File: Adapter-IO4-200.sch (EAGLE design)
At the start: 3 parts, among them X1 MSTBA6

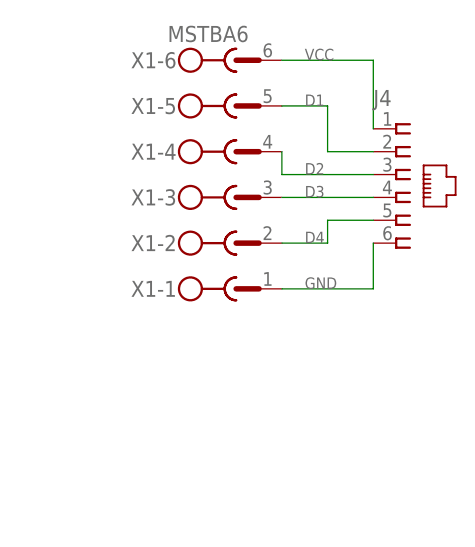
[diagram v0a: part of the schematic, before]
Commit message: added values for connectors
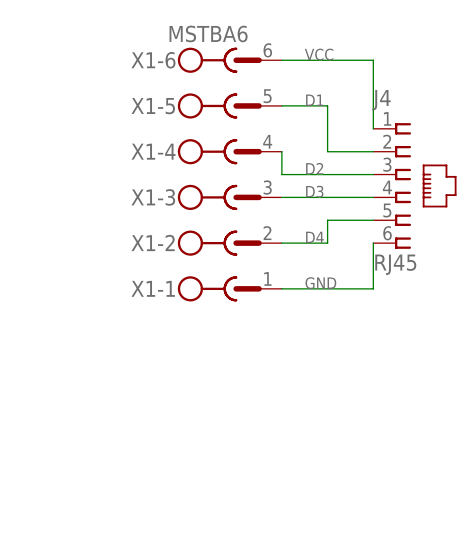
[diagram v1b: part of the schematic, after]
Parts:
- J4: value (none) -> RJ45
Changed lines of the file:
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@@
 <part name="FRAME1" library="SparkFun" deviceset="FRAME-LETTER" device=""/>
 <part name="U$1" library="SparkFun" deviceset="OSHW-LOGO" device="M"/>
-<part name="J4" library="SPCoast" deviceset="CONNECTOR-RJ25" device="-6P6C"/>
+<part name="J4" library="SPCoast" deviceset="CONNECTOR-RJ25" device="-6P6C" value="RJ45"/>
 <part name="X1" library="con-phoenix-508" deviceset="MSTBA6" device=""/>
 </parts>

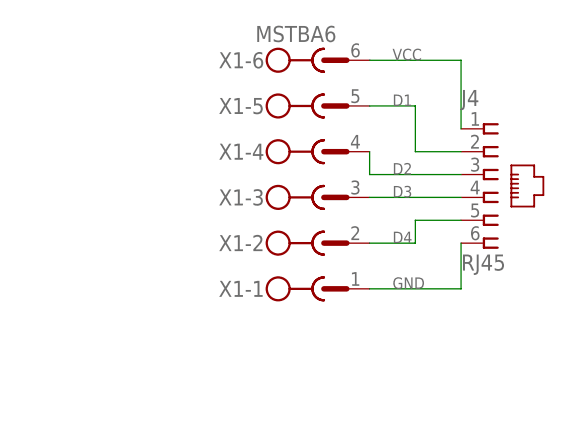
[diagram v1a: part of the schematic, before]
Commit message: normalized values
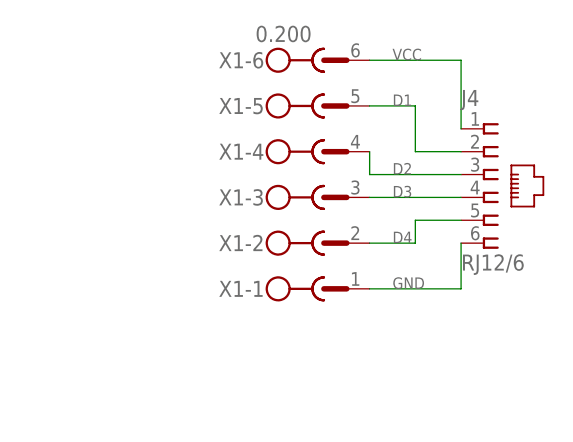
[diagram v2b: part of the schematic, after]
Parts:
- J4: value RJ45 -> RJ12/6
- U$1: value OSHW-LOGOM -> OSHW
- X1: value MSTBA6 -> 0.200
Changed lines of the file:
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@@
 <parts>
 <part name="FRAME1" library="SparkFun" deviceset="FRAME-LETTER" device=""/>
-<part name="U$1" library="SparkFun" deviceset="OSHW-LOGO" device="M"/>
-<part name="J4" library="SPCoast" deviceset="CONNECTOR-RJ25" device="-6P6C" value="RJ45"/>
-<part name="X1" library="con-phoenix-508" deviceset="MSTBA6" device=""/>
+<part name="U$1" library="SparkFun" deviceset="OSHW-LOGO" device="M" value="OSHW"/>
+<part name="J4" library="SPCoast" deviceset="CONNECTOR-RJ25" device="-6P6C" value="RJ12/6"/>
+<part name="X1" library="con-phoenix-508" deviceset="MSTBA6" device="" value="0.200"/>
 </parts>
 <sheets>
